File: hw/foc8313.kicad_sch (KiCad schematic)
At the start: 69 parts, among them J1 Tag Connect, J2 Aux, J3 CAN, J4 CAN, P1 USB_C_Plug, SW1 SW_SPST, SW2 SW_SPST, U1 LMR36015SFBRNXR, U2 XC6206P332MR, U3 DRV8313PWP, U4 AS5047D, U4 STM32F103CBTx, U6 ZD24C08AE1-STGMT, X1 X322516MLB4SI

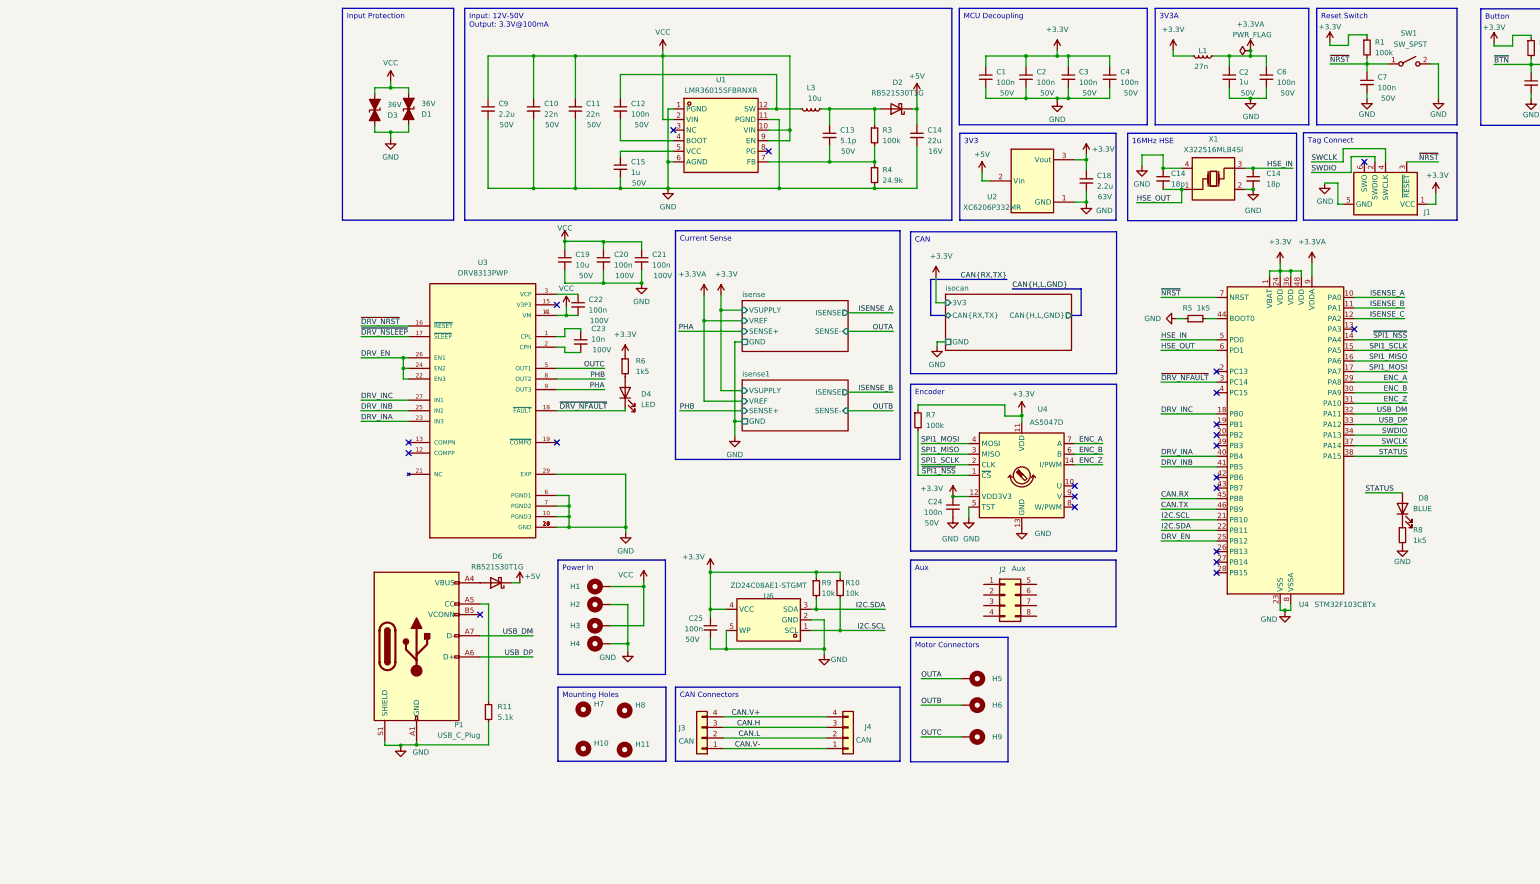
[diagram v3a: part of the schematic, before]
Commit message: [Hw] USBC fixes, 3 wire can, encoder and comms headers
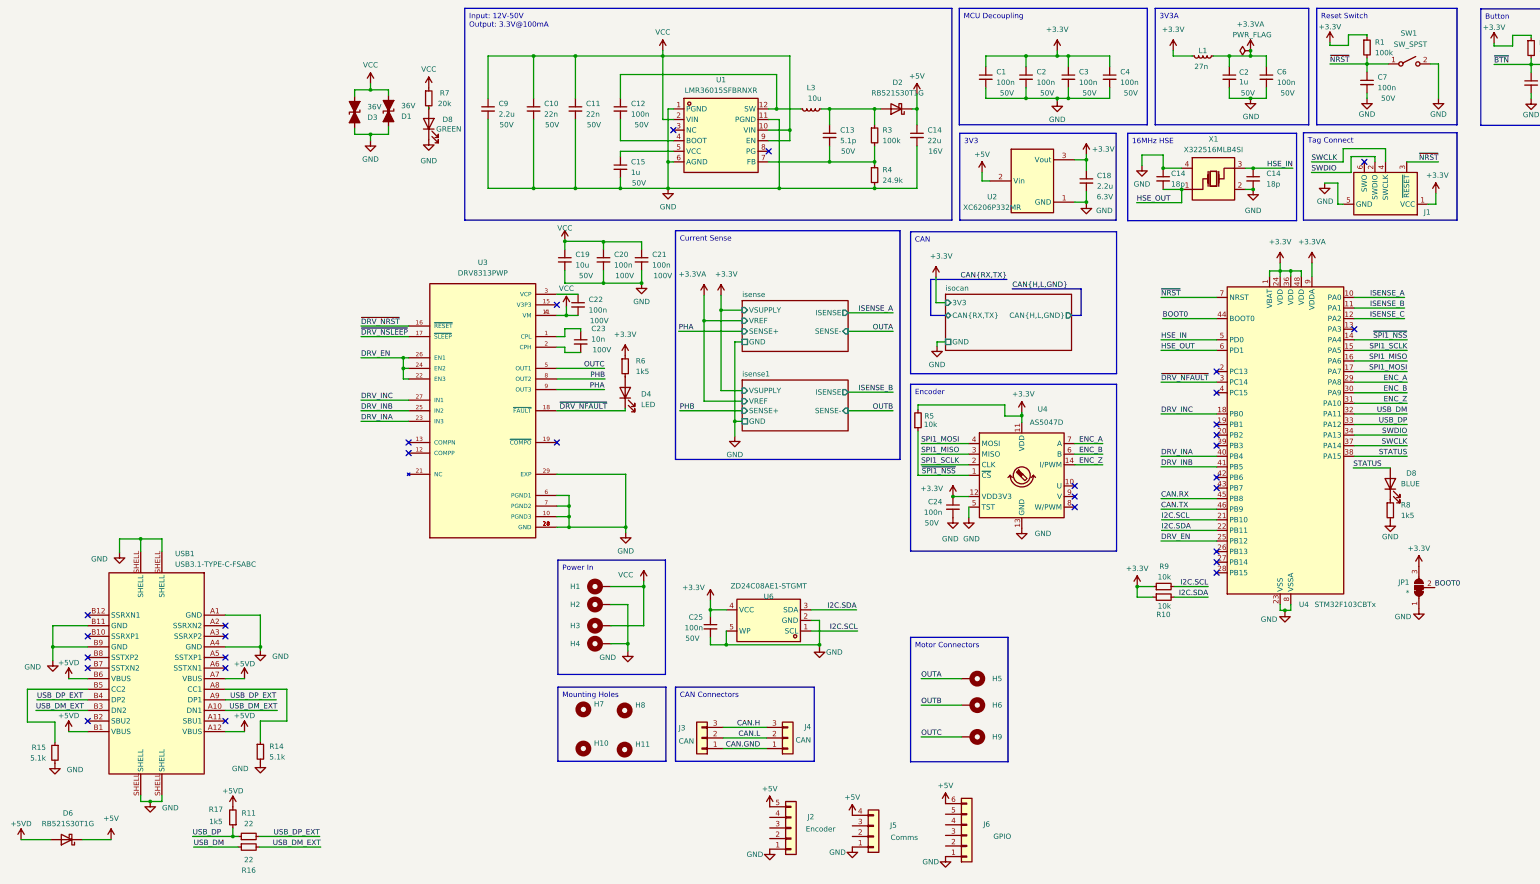
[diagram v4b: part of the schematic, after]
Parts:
- removed J2: Aux, Connector_PinHeader_1.00mm:PinHeader_2x04_P1.00mm_Horizontal, symbol Connector_Generic:Conn_02x04_Top_Bottom
- removed P1: USB_C_Plug, easyeda:USB-3.1-SMD_USB3.1-TYPE-C-FSABC, symbol Connector:USB_C_Plug_USB2.0
- added D8: GREEN, LED_SMD:LED_0402_1005Metric, symbol Device:LED
- added J2: Encoder, easyeda:CONN-SMD_AFC10-S03QCA-00, symbol Connector_Generic:Conn_01x05
- added J5: Comms, easyeda:CONN-SMD_AFC10-S03QCA-00, symbol Connector_Generic:Conn_01x04
- added J6: GPIO, easyeda:CONN-SMD_AFC10-S03QCA-00, symbol Connector_Generic:Conn_01x06
- added JP1: *, Jumper:SolderJumper-3_P1.3mm_Bridged2Bar12_Pad1.0x1.5mm, symbol Jumper:SolderJumper_3_Bridged12
- added R14, R15: 5.1k, Resistor_SMD:R_0402_1005Metric, symbol Device:R_Small
- added R16: 22, Resistor_SMD:R_0402_1005Metric, symbol Device:R_Small
- added R17: 1k5, Resistor_SMD:R_0402_1005Metric, symbol Device:R_Small
- added USB1: USB3.1-TYPE-C-FSABC, easyeda:USB-3.1-SMD_USB3.1-TYPE-C-FSABC, symbol easyeda:USB3.1-TYPE-C-FSABC
- C18: footprint Capacitor_SMD:C_0805_2012Metric -> Capacitor_SMD:C_0402_1005Metric; LCSC C377773 -> C12530; Rating 63V -> 6.3V
- J3, J4: footprint easyeda:CONN-SMD_4P-P1.00_INCP_IPCW100W14XXXXR -> easyeda:CONN-SMD_AFC10-S03QCA-00; symbol Connector_Generic:Conn_01x04 -> Connector_Generic:Conn_01x03
- R11: value 5.1k -> 22; LCSC C25905 -> C25092
- R5: value 1k5 -> 10k; LCSC C25867 -> C25744
- R7: value 100k -> 20k; LCSC C25741 -> C25765
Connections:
- net +3.3V: now also JP1.3 (B)
- net +3V3: now also R5.2; no longer R7.1
- net +5V: now also J2.5 (Pin_5), J5.4 (Pin_4), J6.6 (Pin_6)
- net GND: now also D8.1 (K), J2.1 (Pin_1), J5.1 (Pin_1), J6.1 (Pin_1), JP1.1 (A), R14.2, R15.2, USB1.A1 (GND), USB1.A4 (GND), USB1.B11 (GND), USB1.B9 (GND), USB1.SHELL; no longer R11.2, R5.1
- net I2C.SCL: now also R9.2; no longer R10.2
- net I2C.SDA: now also R10.2; no longer R9.2
- net USB_DM: now also R16.1
- net USB_DP: now also R11.1, R17.1
- net VCC: now also R7.1
- net ~{SPI1_NSS}: now also R5.1; no longer R7.2
- net BOOT0: now reaches U4.44 (BOOT0)
- net BOOT0: now also JP1.2 (C); no longer R5.2
- net +5VD: now reaches D6.2 (A)
- net +5VD: now also R17.2, USB1.A12 (VBUS), USB1.A7 (VBUS), USB1.B1 (VBUS), USB1.B6 (VBUS)
- removed net CAN.V+: J3.4 (Pin_4), J4.4 (Pin_4)
- net CAN.V- renamed CAN.GND
- new net: R14.1, USB1.A8 (CC1)
- new net: D8.2 (A), R7.2
- new net: R15.1, USB1.B5 (CC2)
- new net USB_DM_EXT: R16.2, USB1.A10 (DN1), USB1.B3 (DN2)
- new net USB_DP_EXT: R11.2, USB1.A9 (DP1), USB1.B4 (DP2)
- no-connect marks 22 -> 31
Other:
- moved on the sheet: D1, D3, D8, R10, R8, R9

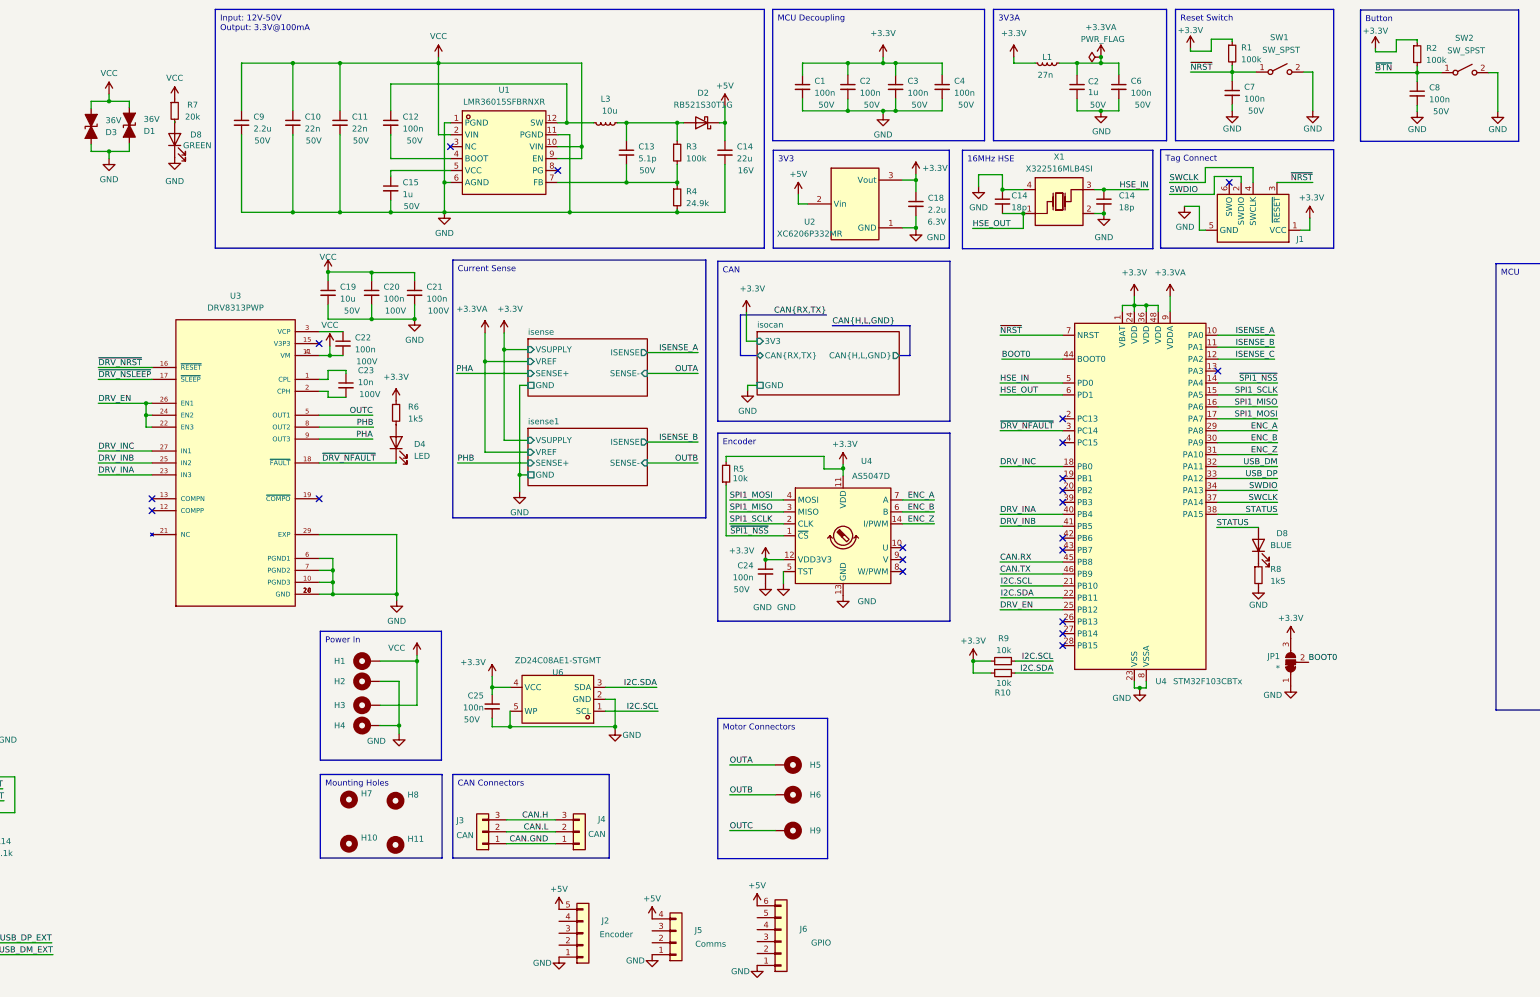
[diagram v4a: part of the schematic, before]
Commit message: [Hw] Optimised pin out for routing, new layout
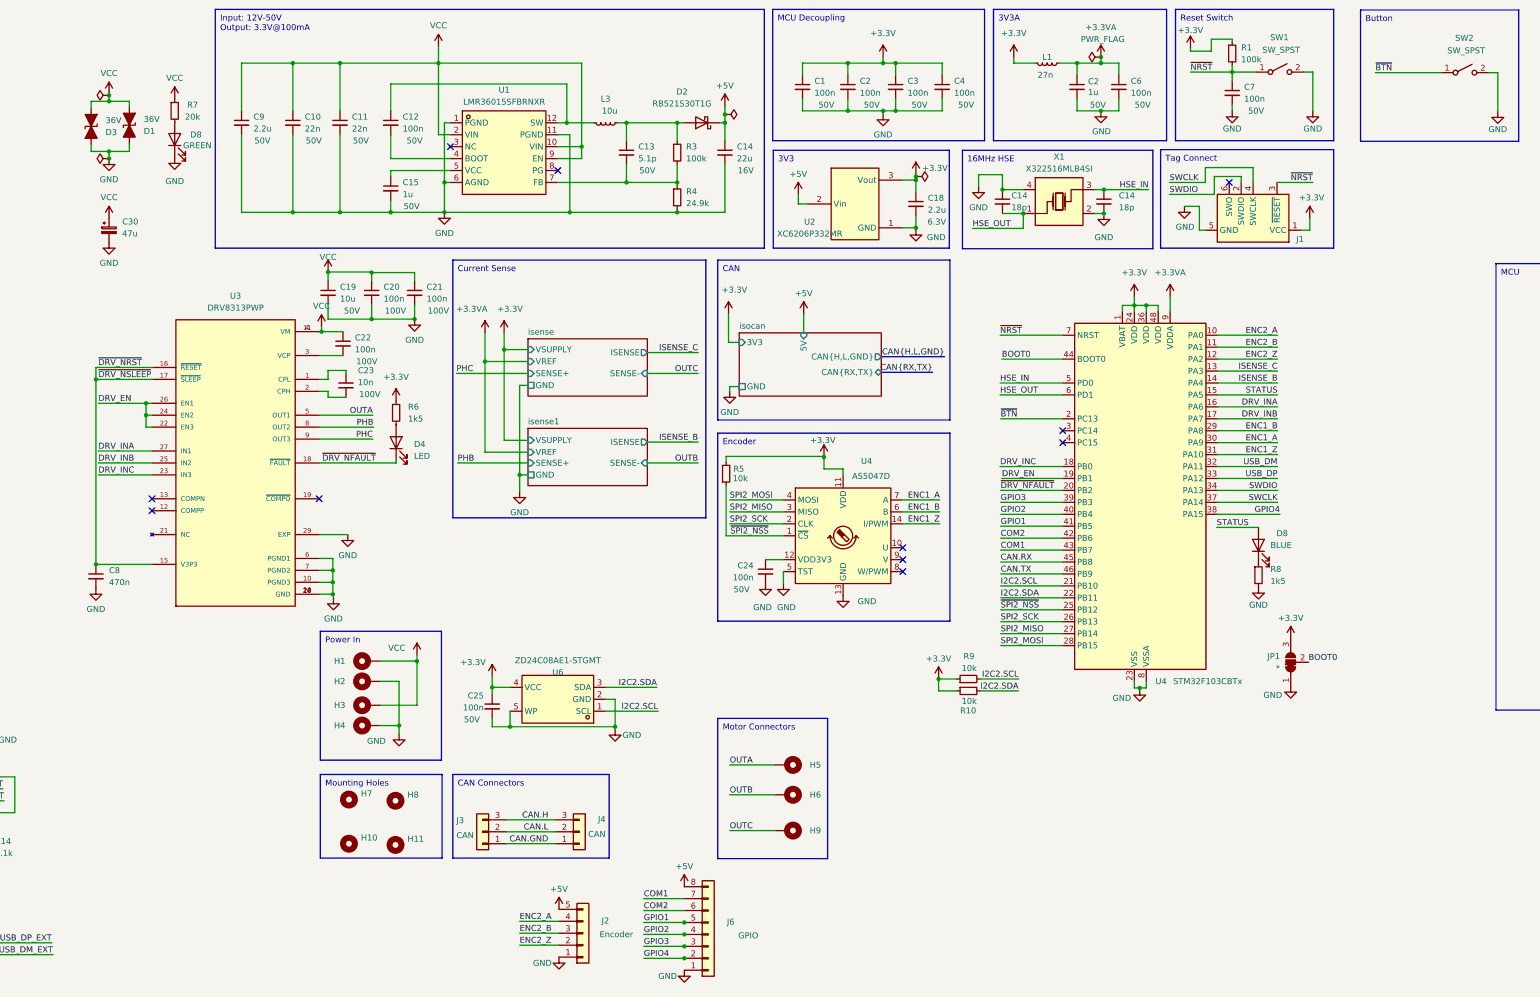
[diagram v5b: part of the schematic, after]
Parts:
- removed J5: Comms, easyeda:CONN-SMD_AFC10-S03QCA-00, symbol Connector_Generic:Conn_01x04
- removed R2: 100k, Resistor_SMD:R_0402_1005Metric, symbol Device:R_Small
- added C30: 47u, Capacitor_SMD:CP_Elec_6.3x5.4, symbol Device:C_Polarized_Small
- C8: value 100n -> 470n; LCSC C307331 -> C107012; Rating 50V -> (none)
- J2: footprint easyeda:CONN-SMD_AFC10-S03QCA-00 -> easyeda:CONN-SMD_5P-P1.00_MEGASTAR_ZX-SH1.0-5PWT; LCSC Part C189895 -> C7430447
- J6: footprint easyeda:CONN-SMD_AFC10-S03QCA-00 -> easyeda:CONN-SMD_8P-P1.00_MEGASTAR_ZX-SH1.0-8PWT; symbol Connector_Generic:Conn_01x06 -> Connector_Generic:Conn_01x08; LCSC Part C189895 -> C7430450
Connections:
- net ISENSE_A is gone; now on net ENC2_A: U4.10 (PA0)
- net ~{DRV_NSLEEP} is gone; now on net ~{DRV_NRST}: U3.17 (~{SLEEP})
- net +3.3V: now also R5.2, U4.11 (VDD)
- net +3V3: no longer C24.1, R5.2, U4.11 (VDD), U4.12 (VDD3V3)
- net +5V: now also J6.8 (Pin_8); no longer J6.6 (Pin_6)
- net DRV_EN: now also U4.19 (PB1); no longer U4.25 (PB12)
- net DRV_INA: now also U3.27 (IN1), U4.16 (PA6); no longer U3.23 (IN3), U4.40 (PB4)
- net DRV_INB: now also U4.17 (PA7); no longer U4.41 (PB5)
- net DRV_INC: now also U3.23 (IN3); no longer U3.27 (IN1)
- net GND: now also C30.2
- net ISENSE_B: now also U4.14 (PA4); no longer U4.11 (PA1)
- net ISENSE_C: now also U4.13 (PA3); no longer U4.12 (PA2)
- net OUTA: now also U3.5 (OUT1)
- net OUTC: no longer U3.5 (OUT1)
- net STATUS: now also U4.15 (PA5); no longer U4.38 (PA15)
- net VCC: now also C22.1, C30.1; no longer C22.2
- net ~{BTN}: now also U4.2 (PC13); no longer C8.1
- net ~{DRV_NFAULT}: now also U4.20 (PB2); no longer U4.3 (PC14)
- net ~{DRV_NRST}: now also C8.1, U3.15 (V3P3)
- net SPI2_SCK: now reaches U4.26 (PB13)
- net SPI2_SCK: now also U4.2 (CLK)
- net SPI2_MISO: now reaches U4.27 (PB14)
- net SPI2_MISO: now also U4.3 (MISO)
- net SPI2_MOSI: now reaches U4.28 (PB15)
- net SPI2_MOSI: now also U4.4 (MOSI)
- net GPIO3: now reaches U4.39 (PB3)
- net GPIO3: now also J6.3 (Pin_3)
- net COM2: now reaches U4.42 (PB6)
- net COM2: now also J6.6 (Pin_6)
- net COM1: now reaches U4.43 (PB7)
- net COM1: now also J6.7 (Pin_7)
- net GPIO4: now reaches J6.2 (Pin_2)
- net GPIO4: now also U4.38 (PA15)
- net GPIO2: now reaches J6.4 (Pin_4)
- net GPIO2: now also U4.40 (PB4)
- net GPIO1: now reaches J6.5 (Pin_5)
- net GPIO1: now also U4.41 (PB5)
- net at U3.3 (VCP): now also C22.2; no longer C22.1
- net ENC2_Z: now reaches J2.2 (Pin_2)
- net ENC2_Z: now also U4.12 (PA2)
- net ENC2_B: now reaches J2.3 (Pin_3)
- net ENC2_B: now also U4.11 (PA1)
- net ENC2_A: now reaches J2.4 (Pin_4)
- net ENC_A renamed ENC1_A
- net ENC1_A: now also U4.30 (PA9); no longer U4.29 (PA8)
- net ENC_B renamed ENC1_B
- net ENC1_B: now also U4.29 (PA8); no longer U4.30 (PA9)
- net ENC_Z renamed ENC1_Z
- net I2C.SCL renamed I2C2.SCL
- net I2C.SDA renamed I2C2.SDA
- net PHA renamed PHC
- removed net SPI1_MISO: U4.16 (PA6), U4.3 (MISO)
- removed net SPI1_MOSI: U4.17 (PA7), U4.4 (MOSI)
- removed net SPI1_SCLK: U4.15 (PA5), U4.2 (CLK)
- net ~{SPI1_NSS} renamed ~{SPI2_NSS}
- net ~{SPI2_NSS}: now also U4.25 (PB12); no longer U4.14 (PA4)
- new net: C24.1, U4.12 (VDD3V3)
- no-connect marks 31 -> 21
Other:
- sheet isocan ports: added 5V; removed none
- moved on the sheet: R10, R9

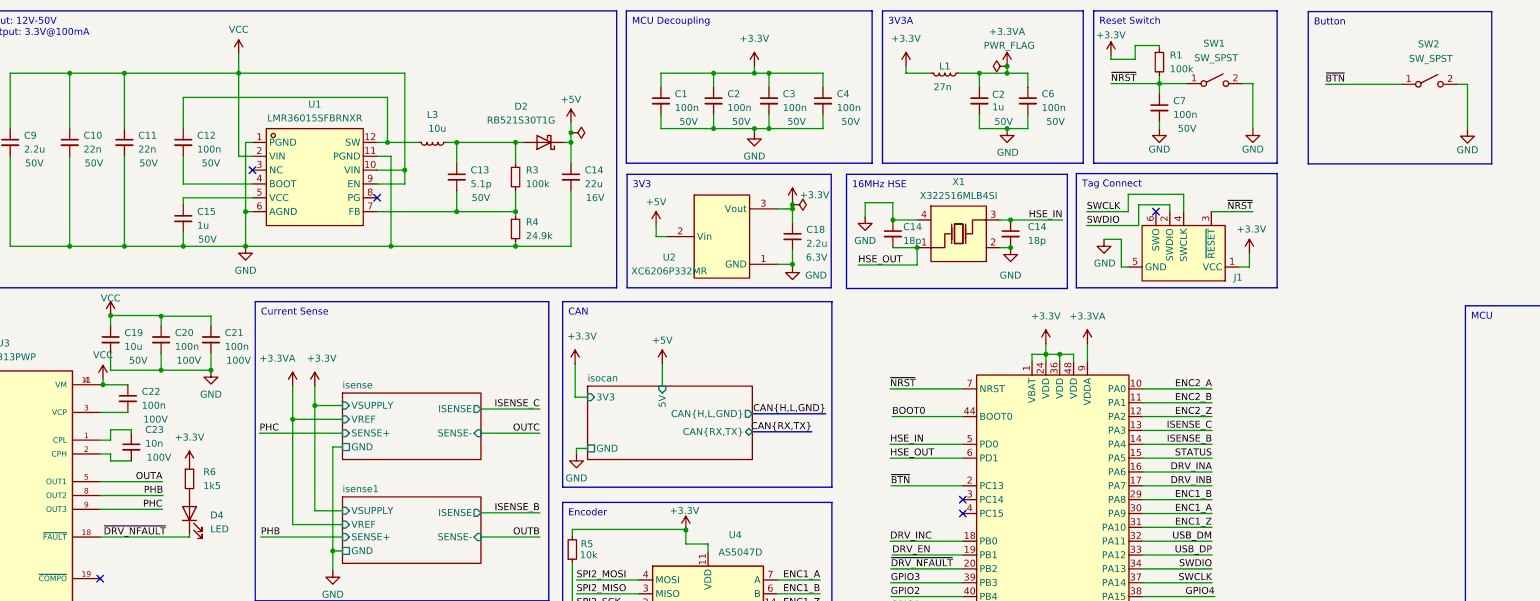
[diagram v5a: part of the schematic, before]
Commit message: [Hw] Routing topology complete
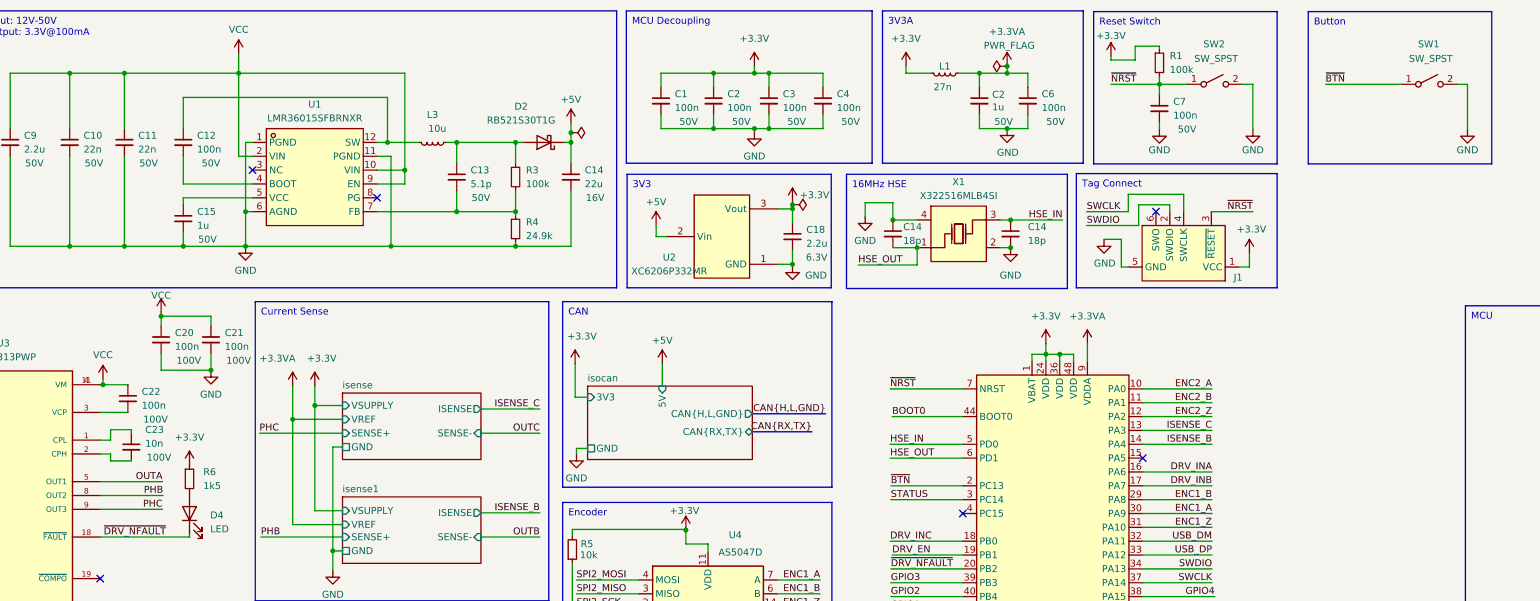
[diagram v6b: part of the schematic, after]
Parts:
- removed C19: 10u, Capacitor_SMD:C_1206_3216Metric, symbol Device:C_Small
- C14: footprint Resistor_SMD:R_0805_2012Metric -> Capacitor_SMD:C_0805_2012Metric
- C30: footprint Capacitor_SMD:CP_Elec_6.3x5.4 -> Capacitor_SMD:CP_Elec_5x5.7; LCSC C131122 -> C7471868
- H1, H2, H3, H4: footprint local_lib:2x5 -> local_lib:2x4
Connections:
- net STATUS: now also U4.3 (PC14); no longer U4.15 (PA5)
- net ~{BTN}: now also SW1.1 (A); no longer SW2.1 (A)
- net ~{NRST}: now also SW2.1 (A); no longer SW1.1 (A)
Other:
- moved on the sheet: SW1, SW2
